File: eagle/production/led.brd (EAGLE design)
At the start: 48 x 84 mm, 19 parts, among them Q1 TIP120, Q2 TIP120, Q3 TIP120, U1 ATMEGA328P_PDIP

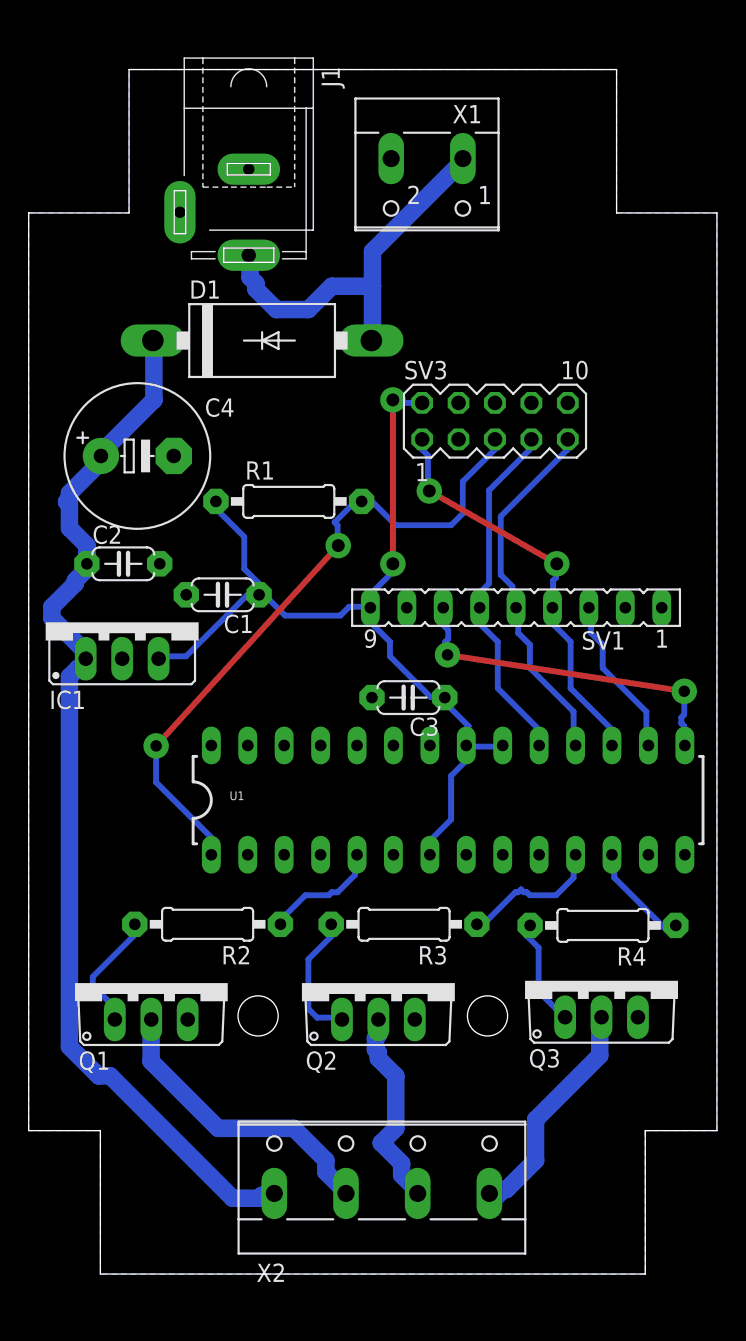
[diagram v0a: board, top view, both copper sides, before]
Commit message: [Eagle] Fixed board
Signed-off-by: Roman3349 <ondracek.roman@centrum.cz>
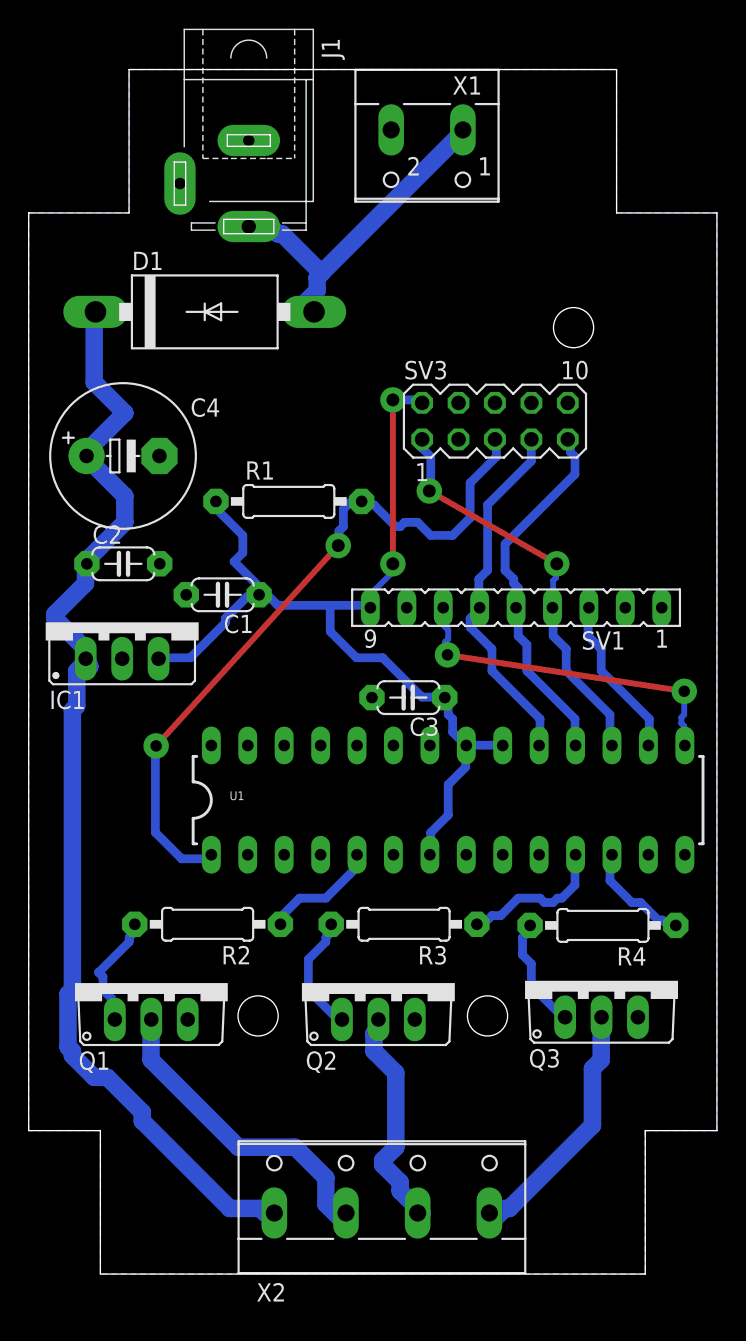
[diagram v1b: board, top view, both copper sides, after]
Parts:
- moved D1 4.47 mm to (12.3, 67.1)
- moved J1 2.00 mm to (15.3, 76.0)
- moved X1 2.00 mm to (27.8, 78.5)
- moved X2 1.36 mm to (24.6, 5.53)
- moved C4 1.00 mm to (6.58, 57.0)
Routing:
- net +12V: track 74.4 -> 78.3 mm
- net N$3: track 27.3 -> 24.1 mm
- net N$5: track 46.5 -> 49.6 mm
- net +5V: track 67.0 -> 69.8 mm
- net N$10: track 20.9 -> 22.7 mm
- net N$1: track 16.5 -> 18.3 mm
- net N$9: track 14.4 -> 16.1 mm
- net N$15: track 9.26 -> 8.48 mm
- net N$14: track 24.5 -> 25.2 mm
- net N$6: track 28.5 -> 29.2 mm

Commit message: Updated schema and board
Signed-off-by: Roman3349 <ondracek.roman@centrum.cz>
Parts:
- added C5, C6: 18p, rcl:C050-024X044
- added Q4: 16MHz, crystal:HC49/S
- C2: value 330n -> 100n
- C4: value 680u -> 470u
- R1: device resistor:0207/10 -> rcl:0207/10
- moved C3 6.07 mm to (21.2, 43.3)
- moved Q1 5.76 mm to (12.7, 16.3)
- moved C1 5.26 mm to (14.3, 52.6)
- moved U1 4.96 mm to (25.1, 35.9)
- moved Q3 4.25 mm to (39.0, 16.3)
- moved Q2 4.12 mm to (25.4, 16.3)
- moved R3 4.03 mm to (27.2, 20.5), turned to 210 degrees
- moved R1 4.03 mm to (22.1, 54.8)
- moved SV3 3.77 mm to (29.3, 61.5)
- moved R4 3.63 mm to (36.6, 23.1), turned to 270 degrees
- moved C2 3.00 mm to (6.60, 52.5)
- moved C4 3.00 mm to (6.58, 60.0)
- moved IC1 3.00 mm to (6.52, 48.5)
- moved R2 2.89 mm to (10.2, 22.6), turned to 270 degrees
- moved D1 2.10 mm to (11.7, 69.1)
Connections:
- new net S$1: C6.2, Q4.1, U1.10
- new net S$2: C5.2, Q4.2, U1.9
- net GND: now also C5.1, C6.1, SV3.6, SV3.8
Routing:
- net S$1: track 0.00 -> 17.9 mm
- net S$2: track 0.00 -> 12.8 mm
- net +5V: track 69.8 -> 57.5 mm
- net N$10: track 22.7 -> 14.4 mm
- net GND: track 0.00 -> 7.62 mm
- net +12V: track 78.3 -> 71.8 mm
- net N$8: track 24.4 -> 18.5 mm
- net N$1: track 18.3 -> 12.5 mm
- net N$9: track 16.1 -> 10.3 mm
- net N$2: track 25.7 -> 20.8 mm
- net N$7: track 11.4 -> 6.84 mm
- net N$14: track 25.2 -> 20.8 mm
- net N$15: track 8.48 -> 4.21 mm
- net N$4: track 8.19 -> 3.94 mm
- net N$11: track 7.75 -> 3.82 mm
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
